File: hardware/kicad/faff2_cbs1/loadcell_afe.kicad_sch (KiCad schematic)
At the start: 0 parts

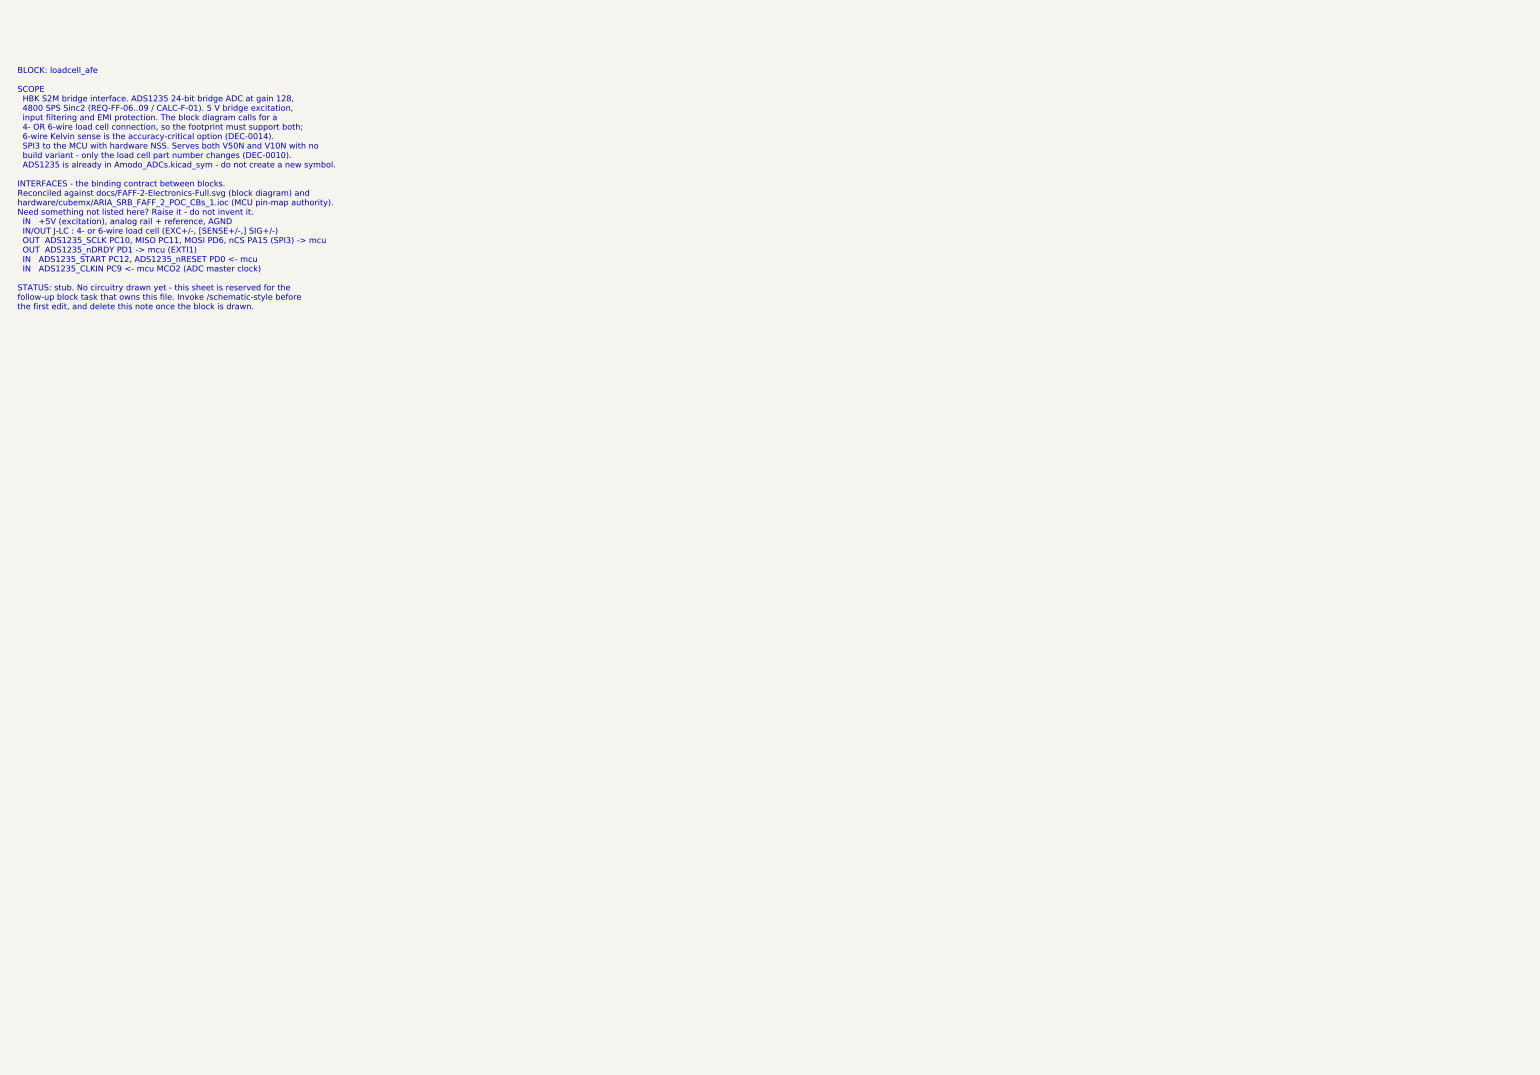
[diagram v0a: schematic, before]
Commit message: loadcell_afe: ADS1235 bridge AFE, 5 V ratiometric excitation, 4/6-wire S2M
Draws the load cell analog front end per REQ-FF-01..13 and REQ-AR-08/09,
at the prelim-calc operating point (gain 128, 4800 SPS, Sinc2, FSR
+/-39.06 mV against a +/-10 mV bridge output, 2.4 uVpp input noise).

  - J501 (Phoenix 1729076, 8-way 5 mm screw terminal) takes the HBK S2M
    six-wire cable plus its screen. R506/R507 are DNP 0R links that tie
    SENSE+/- to EXC+/- for a 4-wire cell; default build is 6-wire per
    DEC-0014.
  - Excitation is the +5VA analog rail through R508, with R509 in the
    bridge return: either link isolates the bridge or takes a meter.
  - Signal and reference filters are the ADS1235 datasheet figure 84
    reference design (100R 0.1% per leg, 1 nF C0G common mode, 10 nF C0G
    differential) with deliberately matched corner frequencies. SENSE+/-
    drive REFP0/REFN0, so the measurement is ratiometric and excitation
    drift cancels. R505 (100k) is the datasheet reference monitor.
  - AIN4/AIN5 carry SIG+/SIG-; AIN0..AIN3 are biased to AVDD through 10k
    per datasheet 9.1.3.
  - SPI3, START, nRESET and nDRDY use the .ioc net names. The 47R series
    resistors are both the datasheet series terminators and the SPI3
    isolation links. CLKIN comes from MCO2 through R520, with a DNP R521
    that grounds CLKIN to select the ADC internal oscillator instead.
  - Test provisions per TEST_PLAN.md section 4: test points on
    excitation, sense and reference, U.FL on both ADC-side SIG nodes,
    hooks on every MCU-facing net and two GND hooks.

Datasheets for ADS1235 (SBAS824), ADS1120 (SBAS535D) and the HBK S2M
(B03594) are added under datasheets/ - all three pin maps and component
values in this sheet are taken from them, not from memory.

Verification: kicad-cli 9.0.8 ERC at --severity-all over the whole
project reports only the 8 hier_label_mismatch errors that DEC-0009
makes unavoidable while the root sheet is unwired; the bundled overlap
checker is clean;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
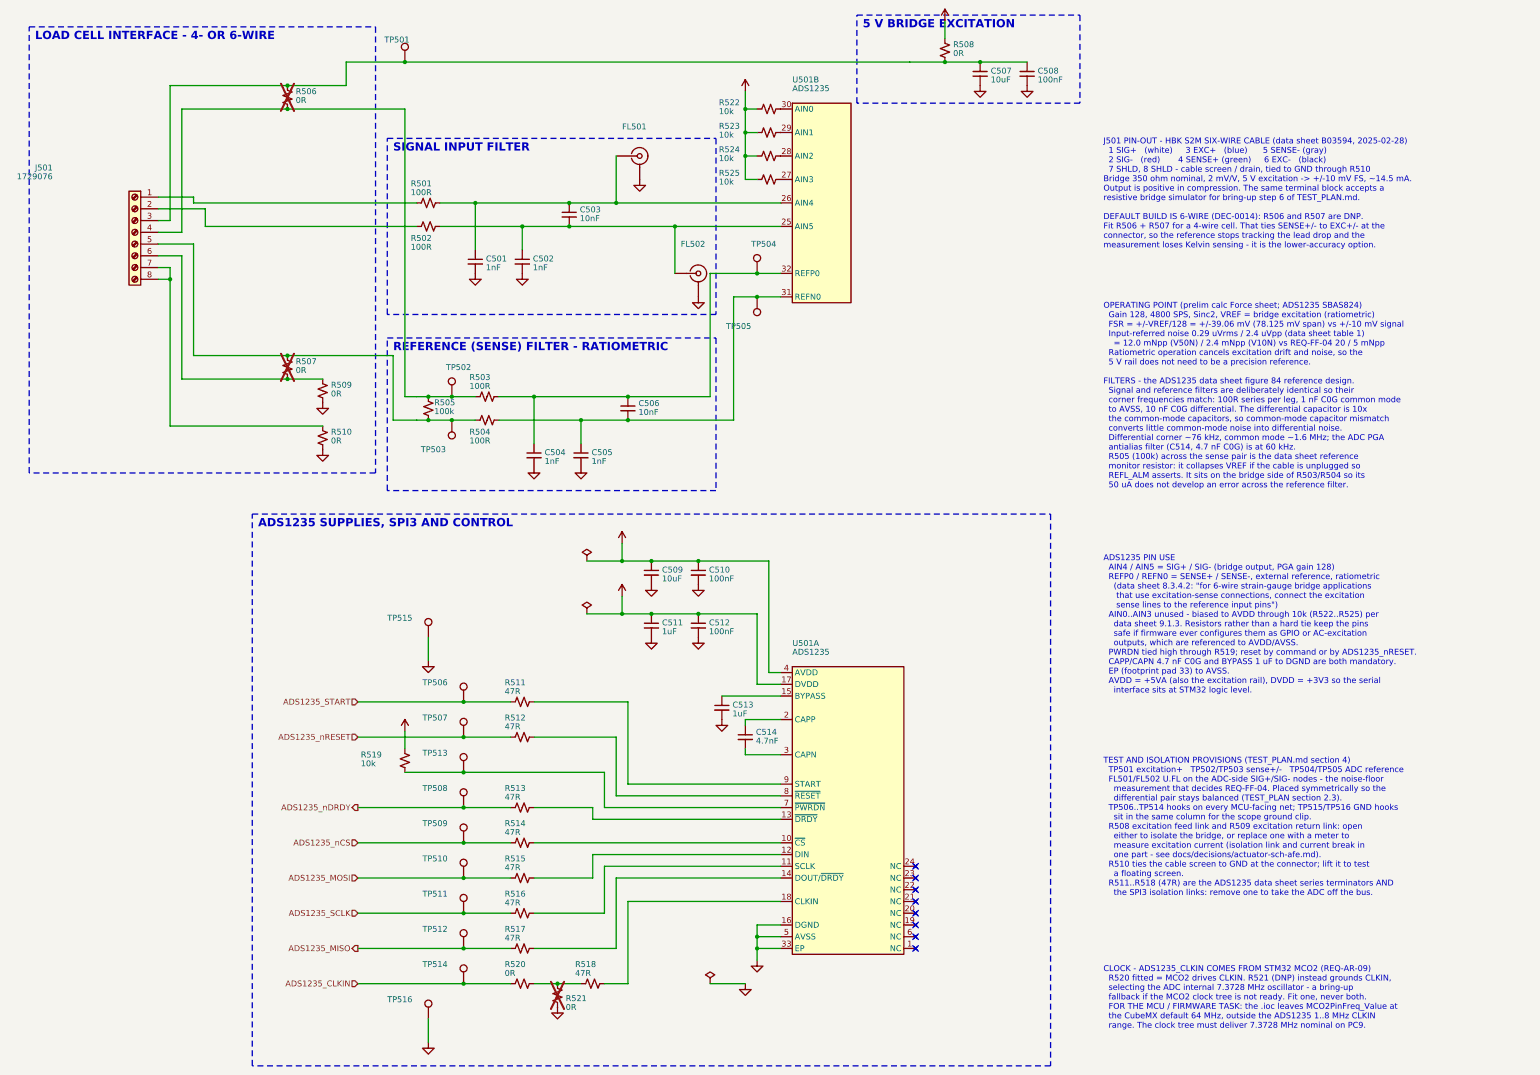
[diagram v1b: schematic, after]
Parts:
- added C501, C502, C504, C505: 1nF, Amodo:C_0603_1608Metric, symbol Amodo_Capacitors:CAP_MLCC_1nF_0603_1%_200V_C0G
- added C503, C506: 10nF, Amodo:C_0603_1608Metric, symbol Amodo_Capacitors:CAP_MLCC_10nF_0603_5%_100V
- added C507, C509: 10uF, Amodo:C_0805_2012Metric, symbol Amodo_Capacitors:CAP_MLCC_10uF_0805_20%_25V
- added C508, C510, C512: 100nF, Amodo:C_0402_1005Metric, symbol Amodo_Capacitors:CAP_MLCC_100nF_0402_10%_50V
- added C511, C513: 1uF, Amodo:C_0603_1608Metric, symbol Amodo_Capacitors:CAP_MLCC_1uF_0603_10%_16V
- added C514: 4.7nF, Amodo:C_0805_2012Metric, symbol Amodo_Capacitors:CAP_MLCC_4.7nF_0805_5%_200V_C0G
- added FL501, FL502: CONUFL001-SMD, Amodo:CONUFL001-SMD, symbol Amodo_Connectors:CONUFL001-SMD
- added J501: 1729076, Amodo:1729076, symbol Amodo_Connectors:1729076
- added R501, R502, R503, R504: 100R, Amodo:R_0603_1608Metric, symbol Amodo_Resistors:RES_TNF_100R_0603_0.1%
- added R505: 100k, Amodo:R_0603_1608Metric, symbol Amodo_Resistors:RES_TF_100k_0603
- added R506, R507, R508, R509, R510, R520, R521: 0R, Amodo:R_0603_1608Metric, symbol Amodo_Resistors:RES_TF_0R_0603
- added R511, R512, R513, R514, R515, R516, R517, R518: 47R, Amodo:R_0603_1608Metric, symbol Amodo_Resistors:RES_TF_47R_0603
- added R519, R522, R523, R524, R525: 10k, Amodo:R_0603_1608Metric, symbol Amodo_Resistors:RES_TF_10k_0603
- added TP501, TP506, TP507, TP508, TP509, TP510, TP511, TP512, TP513, TP514, TP515, TP516: TestPoint, Amodo:KeystoneMiniatureTestLoop, symbol Amodo_Connectors:TestPointHook
- added TP502, TP503, TP504, TP505: TestPoint, Amodo:TestPoint_Pad_D1.0mm, symbol Amodo_Connectors:TestPoint
- added U501: ADS1235, Amodo:VQFN RHB 32 5x5 mm 0.5 pitch, symbol Amodo_ADCs:ADS1235
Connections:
- new net: R514.2, U501.10 (~{CS})
- new net: J501.5, R504.1, R505.2, R507.1, TP503.1
- new net: J501.6, R507.2, R509.1
- new net: C507.1, C508.1, J501.3, R506.1, R508.2, TP501.1
- new net: R523.2, U501.29 (AIN1)
- new net: C505.1, C506.2, R504.2, TP505.1, U501.31 (REFN0)
- new net: R522.2, U501.30 (AIN0)
- new net: C502.1, C503.2, FL502.1 (In), R502.2, U501.25 (AIN5)
- new net: J501.1, R501.1
- new net: J501.2, R502.1
- new net: J501.4, R503.1, R505.1, R506.2, TP502.1
- new net: J501.7, J501.8, R510.1
- new net: C504.1, C506.1, R503.2, TP504.1, U501.32 (REFP0)
- new net: R518.1, R520.2, R521.1
- new net: R518.2, U501.18 (CLKIN)
- new net: R517.2, U501.14 (DOUT/~{DRDY})
- new net: R524.2, U501.28 (AIN2)
- new net: C501.1, C503.1, FL501.1 (In), R501.2, U501.26 (AIN4)
- new net: R525.2, U501.27 (AIN3)
- new net: R512.2, U501.8 (~{RESET})
- new net: R511.2, U501.9 (START)
- new net: R515.2, U501.12 (DIN)
- new net: C513.1, U501.15 (BYPASS)
- new net: R516.2, U501.11 (SCLK)
- new net: R513.2, U501.13 (~{DRDY})
- new net: C514.1, U501.2 (CAPP)
- new net: C514.2, U501.3 (CAPN)
- new net: R519.2, TP513.1, U501.7 (~{PWRDN})
- new net +3V3: C511.1, C512.1, R519.1, U501.17 (DVDD)
- new net +5VA: C509.1, C510.1, R508.1, R522.1, R523.1, R524.1, R525.1, U501.4 (AVDD)
- new net ADS1235_CLKIN: R520.1, TP514.1
- new net ADS1235_MISO: R517.1, TP512.1
- new net ADS1235_MOSI: R515.1, TP510.1
- new net ADS1235_SCLK: R516.1, TP511.1
- new net ADS1235_START: R511.1, TP506.1
- new net ADS1235_nCS: R514.1, TP509.1
- new net ADS1235_nDRDY: R513.1, TP508.1
- new net ADS1235_nRESET: R512.1, TP507.1
- new net GND: C501.2, C502.2, C504.2, C505.2, C507.2, C508.2, C509.2, C510.2, C511.2, C512.2, C513.2, FL501.2 (Ext), FL501.3 (Ext), FL502.2 (Ext), FL502.3 (Ext), R509.2, R510.2, R521.2, TP515.1, TP516.1, U501.16 (DGND), U501.33 (EP), U501.5 (AVSS)
- no-connect marks 0 -> 8
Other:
- note added: "5 V BRIDGE EXCITATION"
- note added: "ADS1235 PIN USE AIN4 / AIN5 = SIG+ / SIG- (bridge output, PGA gain 128) REFP0 / REFN0 = SENSE+ / SENSE-, external reference, ratiometric (data sheet 8.3.4.2: "for 6-wire strain-gauge bridge applications that use excitation-sense connections, connect the excitation sense lines to the reference input pins") AIN0..AIN3 unused - biased to AVDD through 10k (R522..R525) per data sheet 9.1.3. Resistors 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"
- note added: "ADS1235 SUPPLIES, SPI3 AND CONTROL"
- note added: "CLOCK - ADS1235_CLKIN COMES FROM STM32 MCO2 (REQ-AR-09) R520 fitted = MCO2 drives CLKIN. R521 (DNP) instead grounds CLKIN, selecting the ADC internal 7.3728 MHz oscillator - a bring-up fallback if the MCO2 clock tree is not ready. Fit one, never both. FOR THE MCU / FIRMWARE TASK: the .ioc leaves MCO2PinFreq_Value at the CubeMX default 64 MHz, outside the ADS1235 1..8 MHz CLKIN range. The clock tr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"
- note added: "J501 PIN-OUT - HBK S2M SIX-WIRE CABLE (data sheet B03594, 2025-02-28) 1 SIG+ (white) 3 EXC+ (blue) 5 SENSE- (gray) 2 SIG- (red) 4 SENSE+ (green) 6 EXC- (black) 7 SHLD, 8 SHLD - cable screen / drain, tied to GND through R510 Bridge 350 ohm nominal, 2 mV/V, 5 V excitation -> +/-10 mV FS, ~14.5 mA. Output is positive in compression. The same terminal block accepts a resistive bridge simulator for br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"
- note added: "LOAD CELL INTERFACE - 4- OR 6-WIRE"
- note added: "OPERATING POINT (prelim calc Force sheet; ADS1235 SBAS824) Gain 128, 4800 SPS, Sinc2, VREF = bridge excitation (ratiometric) FSR = +/-VREF/128 = +/-39.06 mV (78.125 mV span) vs +/-10 mV signal Input-referred noise 0.29 uVrms / 2.4 uVpp (data sheet table 1) = 12.0 mNpp (V50N) / 2.4 mNpp (V10N) vs REQ-FF-04 20 / 5 mNpp Ratiometric operation cancels excitation drift and noise, so the 5 V rail does n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"
- note added: "REFERENCE (SENSE) FILTER - RATIOMETRIC"
- note added: "SIGNAL INPUT FILTER"
- note added: "TEST AND ISOLATION PROVISIONS (TEST_PLAN.md section 4) TP501 excitation+ TP502/TP503 sense+/- TP504/TP505 ADC reference FL501/FL502 U.FL on the ADC-side SIG+/SIG- nodes - the noise-floor measurement that decides REQ-FF-04. Placed symmetrically so the differential pair stays balanced (TEST_PLAN section 2.3). TP506..TP514 hooks on every MCU-facing net; TP515/TP516 GND hooks sit in the same column f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"
- note removed: "BLOCK: loadcell_afe SCOPE HBK S2M bridge interface. ADS1235 24-bit bridge ADC at gain 128, 4800 SPS Sinc2 (REQ-FF-06..09 / CALC-F-01). 5 V bridge excitation, input filtering and EMI protection. The block diagram calls for a 4- OR 6-wire load cell connection, so the footprint must support both; 6-wire Kelvin sense is the accuracy-critical option (DEC-0014). SPI3 to the MCU with hardware NSS. Serve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"

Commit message: temp_sense: two 3-wire Pt1000 channels on one ADS1120; AFE symbol goes local
Draws temp_sense and completes the analog front end. Reasoning, the answer to
OQ-04 and the root-sheet interface list are in docs/decisions/actuator-sch-afe.md.

temp_sense (REQ-EL-07, REQ-AR-10):
  - OQ-04 answered: RTD, not NTC. Pt1000, 3-wire, class A. The ADS1120's two
    matched IDACs exist to excite an RTD ratiometrically and cancel lead
    resistance; a class-A RTD is interchangeable to +/-(0.15 + 0.002|t|) degC
    with no per-part calibration, which an NTC would need to reach 1 degC.
    Pt1000 over Pt100 because every error term here is an error in ohms, and at
    3.85 ohm/degC each costs ten times less in degrees.
  - Both channels share one ADS1120 AND one reference resistor, using the
    datasheet variant (SBAS535D 9.2.2) that routes each IDAC to the pin it
    measures. Its condition - small, well-matched filter resistors - is met with
    100R 0.1%, worth 0.05 degC on a Pt1000.
  - 250 uA IDACs, R707 = 5k 0.05% / 5 ppm, VREF 2.5 V, gain 4. Gain 4 rather
    than 8 keeps the input inside FSR to +200 degC so a probe on warm structure
    cannot silently over-range; resolution is still 0.02 degC. The same board
    takes a Pt100 (the house-stocked probe) with only register changes.
  - Error budget RSS +/-0.28 degC against the 1 degC requirement; the two gain
    terms left out are removed by one-point calibration or IDAC rotation.
  - R708/R709 (DNP) tie the sense lead to the return for a 2-wire probe, which
    keeps the block diagram's "RTD / NTC" option open at lower accuracy.
  - Push-in terminals so a substitute resistor needs no soldering (TEST_PLAN 4).

loadcell_afe: no design change. PWR_FLAGs removed - the power sheets own every
one, and a second flag on a shared rail is a power-output conflict at merge.

Library: AmodoKiCadLib is read-only, so the corrected ADS1235 now lives in
hardware/kicad/faff2_cbs1/faff2_afe.kicad_sym with a sym-lib-table entry, and
the share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
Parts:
- removed U501: ADS1235, Amodo:VQFN RHB 32 5x5 mm 0.5 pitch, symbol Amodo_ADCs:ADS1235
- added U501: ADS1235, Amodo:VQFN RHB 32 5x5 mm 0.5 pitch, symbol faff2_afe:ADS1235
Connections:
- net +3V3: now also U501.17 (DVDD)
- net +5VA: now also U501.4 (AVDD)
- net GND: now also U501.16 (DGND), U501.33 (EP), U501.5 (AVSS)
- net at R514.2: now also U501.10 (~{CS})
- net at R523.2: now also U501.29 (AIN1)
- net at C505.1, C506.2, R504.2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: now also U501.31 (REFN0)
- net at R522.2: now also U501.30 (AIN0)
- net at C502.1, C503.2, FL502.1 (In)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: now also U501.25 (AIN5)
- net at C504.1, C506.1, R503.2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: now also U501.32 (REFP0)
- net at R518.2: now also U501.18 (CLKIN)
- net at R517.2: now also U501.14 (DOUT/~{DRDY})
- net at R524.2: now also U501.28 (AIN2)
- net at C501.1, C503.1, FL501.1 (In)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: now also U501.26 (AIN4)
- net at R525.2: now also U501.27 (AIN3)
- net at R512.2: now also U501.8 (~{RESET})
- net at R511.2: now also U501.9 (START)
- net at R515.2: now also U501.12 (DIN)
- net at C513.1: now also U501.15 (BYPASS)
- net at R516.2: now also U501.11 (SCLK)
- net at R513.2: now also U501.13 (~{DRDY})
- net at C514.1: now also U501.2 (CAPP)
- net at C514.2: now also U501.3 (CAPN)
- net at R519.2, TP513.1: now also U501.7 (~{PWRDN})
